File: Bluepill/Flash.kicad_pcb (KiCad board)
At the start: 2 copper layers, 83.3 x 92.7 mm, 48 parts, among them CON1 GENESIS-CONN, J1 USB_B_Micro, J2 Conn_Bluepill_Left, J3 Conn_Bluepill_right, U1 RT9193, U2 STM32F103C8Tx, U3 4069, U4 74HC590, U5 74LVC245, U6 74HC590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

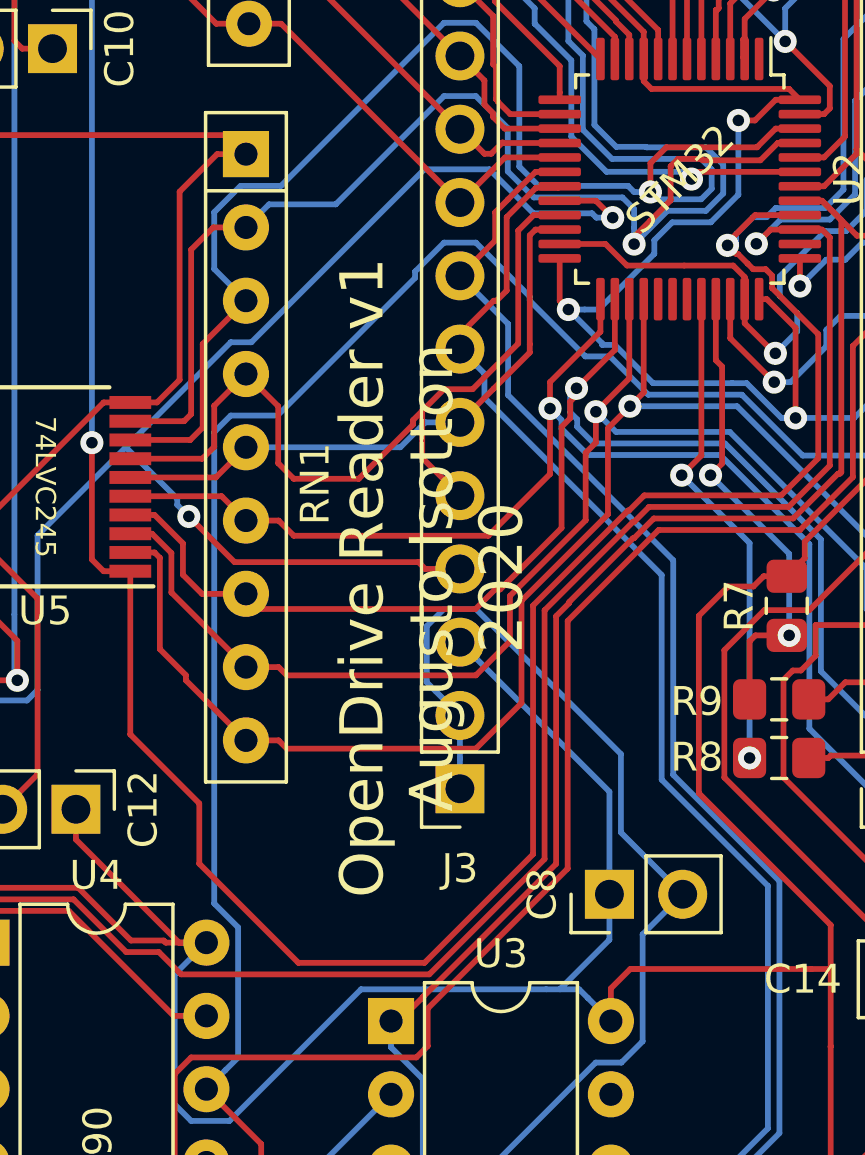
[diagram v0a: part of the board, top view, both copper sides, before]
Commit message: Small silkscreen changes
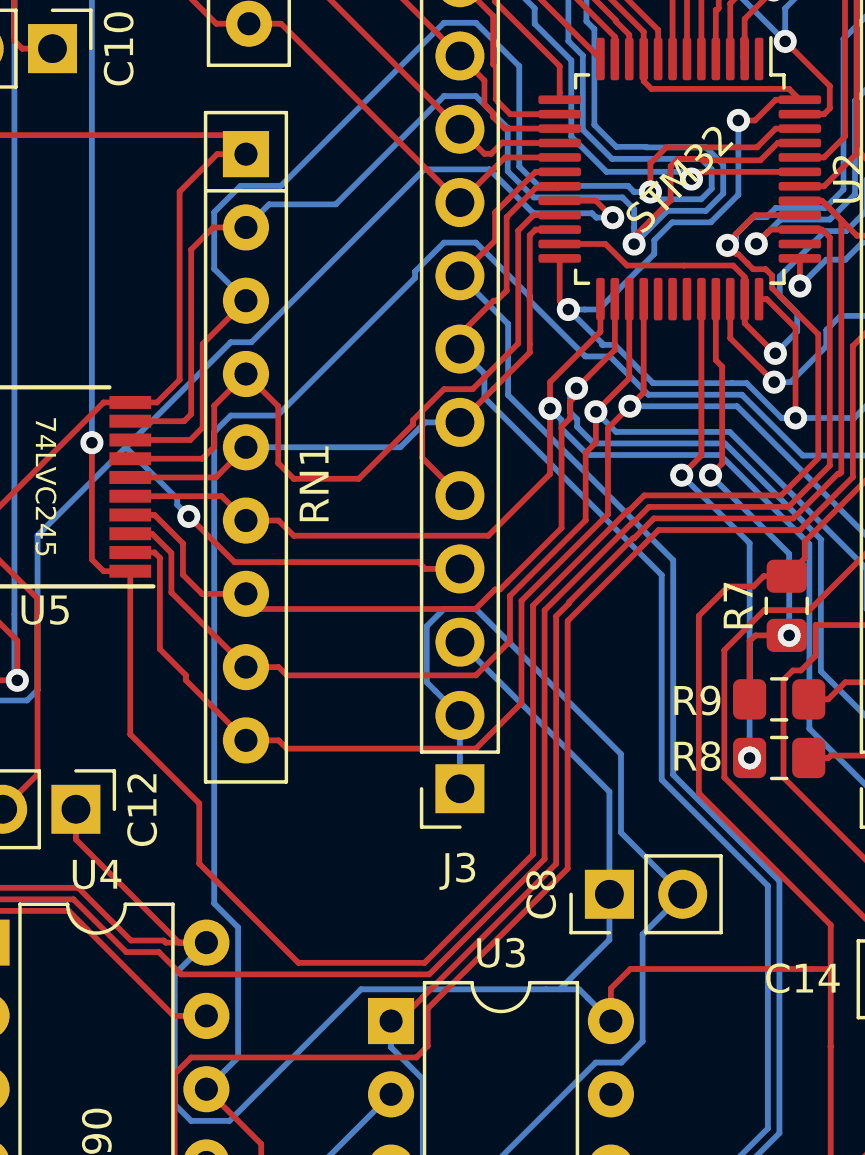
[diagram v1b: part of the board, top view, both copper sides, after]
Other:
- board text removed: "OpenDrive Reader v1 Augusto Isotton 2020"

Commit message: Connected A22 and A23 on the cart connector for SNES support
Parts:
- RN1, RN2, RN3, RN4, RN5, RN8, RN9: value R_Network08 -> 10K
- RN6, RN7: value R_Network08 -> 1K
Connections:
- CON1 pad B10: (no net) -> /A21
- CON1 pad B11: (no net) -> /A22
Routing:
- net /A22: track 5.08 -> 28.8 mm
- net /A21: track 5.08 -> 27.8 mm
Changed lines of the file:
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@@
     (thickness 1.6)
     (drawings 27)
-    (tracks 2072)
+    (tracks 2084)
     (zones 0)
     (modules 48)
@@
       (effects (font (size 1 1) (thickness 0.15)))
     )
-    (fp_text value R_Network08 (at 11.43 2.4 90) (layer F.Fab)
+    (fp_text value 10K (at 11.43 2.4 90) (layer F.Fab)
       (effects (font (size 1 1) (thickness 0.15)))
     )
@@
       (effects (font (size 1 1) (thickness 0.15)))
     )
-    (fp_text value R_Network08 (at 11.43 2.4) (layer F.Fab)
+    (fp_text value 1K (at 11.43 2.4) (layer F.Fab)
       (effects (font (size 1 1) (thickness 0.15)))
     )
@@
     (pad B9 thru_hole circle (at 0 20.32) (size 1.524 1.524) (drill 1.016) (layers *.Cu *.Mask)
       (net 28 /A20))
-    (pad B10 thru_hole circle (at 0 22.86) (size 1.524 1.524) (drill 1.016) (layers *.Cu *.Mask))
-    (pad B11 thru_hole circle (at 0 25.4) (size 1.524 1.524) (drill 1.016) (layers *.Cu *.Mask))
+    (pad B10 thru_hole circle (at 0 22.86) (size 1.524 1.524) (drill 1.016) (layers *.Cu *.Mask)
+      (net 76 /A21))
+    (pad B11 thru_hole circle (at 0 25.4) (size 1.524 1.524) (drill 1.016) (layers *.Cu *.Mask)
+      (net 77 /A22))
     (pad B12 thru_hole circle (at 0 27.94) (size 1.524 1.524) (drill 1.016) (layers *.Cu *.Mask))
     (pad B13 thru_hole circle (at 0 30.48) (size 1.524 1.524) (drill 1.016) (layers *.Cu *.Mask))
@@
       (effects (font (size 1 1) (thickness 0.15)))
     )
-    (fp_text value R_Network08 (at 11.43 2.4 90) (layer F.Fab)
+    (fp_text value 10K (at 11.43 2.4 90) (layer F.Fab)
       (effects (font (size 1 1) (thickness 0.15)))
     )
@@
       (effects (font (size 1 1) (thickness 0.15)))
     )
-    (fp_text value R_Network08 (at 11.43 2.4 90) (layer F.Fab)
+    (fp_text value 10K (at 11.43 2.4 90) (layer F.Fab)
       (effects (font (size 1 1) (thickness 0.15)))
     )
@@
       (effects (font (size 1 1) (thickness 0.15)))
     )
-    (fp_text value R_Network08 (at 11.43 2.4 90) (layer F.Fab)
+    (fp_text value 10K (at 11.43 2.4 90) (layer F.Fab)
       (effects (font (size 1 1) (thickness 0.15)))
     )
@@
       (effects (font (size 1 1) (thickness 0.15)))
     )
-    (fp_text value R_Network08 (at 11.43 2.4 90) (layer F.Fab)
+    (fp_text value 10K (at 11.43 2.4 90) (layer F.Fab)
       (effects (font (size 1 1) (thickness 0.15)))
     )
@@
       (effects (font (size 1 1) (thickness 0.15)))
     )
-    (fp_text value R_Network08 (at 11.43 2.4) (layer F.Fab)
+    (fp_text value 1K (at 11.43 2.4) (layer F.Fab)
       (effects (font (size 1 1) (thickness 0.15)))
     )
@@
       (effects (font (size 1 1) (thickness 0.15)))
     )
-    (fp_text value R_Network08 (at 11.43 2.4 90) (layer F.Fab)
+    (fp_text value 10K (at 11.43 2.4 90) (layer F.Fab)
       (effects (font (size 1 1) (thickness 0.15)))
     )
@@
       (effects (font (size 1 1) (thickness 0.15)))
     )
-    (fp_text value R_Network08 (at 11.43 2.4 90) (layer F.Fab)
+    (fp_text value 10K (at 11.43 2.4 90) (layer F.Fab)
       (effects (font (size 1 1) (thickness 0.15)))
     )
@@
   (segment (start 139.1832 50.6388) (end 140.1356 49.6864) (width 0.2) (layer F.Cu) (net 75))
   (segment (start 92.837 65.3288) (end 97.917 65.3288) (width 0.2) (layer F.Cu) (net 76) (status 30))
+  (segment (start 109.118401 79.502001) (end 109.8804 80.264) (width 0.2) (layer B.Cu) (net 76))
+  (segment (start 108.818399 79.201999) (end 109.118401 79.502001) (width 0.2) (layer B.Cu) (net 76))
+  (segment (start 103.943792 79.201999) (end 108.818399 79.201999) (width 0.2) (layer B.Cu) (net 76))
+  (segment (start 100.28543 75.543637) (end 103.943792 79.201999) (width 0.2) (layer B.Cu) (net 76))
+  (segment (start 100.28543 67.64643) (end 100.28543 75.543637) (width 0.2) (layer B.Cu) (net 76))
+  (segment (start 97.9678 65.3288) (end 100.28543 67.64643) (width 0.2) (layer B.Cu) (net 76))
   (segment (start 92.837 62.7888) (end 97.917 62.7888) (width 0.2) (layer F.Cu) (net 77) (status 30))
+  (segment (start 109.118401 76.962001) (end 109.8804 77.724) (width 0.2) (layer B.Cu) (net 77))
+  (segment (start 108.8136 76.6572) (end 109.118401 76.962001) (width 0.2) (layer B.Cu) (net 77))
+  (segment (start 102.15864 76.6572) (end 108.8136 76.6572) (width 0.2) (layer B.Cu) (net 77))
+  (segment (start 100.68544 75.184) (end 102.15864 76.6572) (width 0.2) (layer B.Cu) (net 77))
+  (segment (start 100.68544 65.50644) (end 100.68544 75.184) (width 0.2) (layer B.Cu) (net 77))
+  (segment (start 97.9678 62.7888) (end 100.68544 65.50644) (width 0.2) (layer B.Cu) (net 77))
   (segment (start 92.837 60.2488) (end 97.917 60.2488) (width 0.2) (layer F.Cu) (net 78) (status 30))
   (segment (start 156.125519 55.2704) (end 157.3276 55.2704) (width 0.2) (layer B.Cu) (net 79))
